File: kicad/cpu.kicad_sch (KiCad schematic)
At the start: 41 parts, among them U1 8088_Max_Mode, U12 8288, U13 SN74PAL16L81N, U145 PAL12L6, U16 7400, U2 8087, U3 XD184000xP, U4 8284, U5 74LS244, U77 74LS04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

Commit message: Fixes to clocks,  keyboard controller stuff.
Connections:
- net CLK_{8288} is gone; now on net CLK_{88}: U12.2 (CLK)
- net CLK_{88}: now also U77.9, U80.1 (I_{0}), U81.3 (I1a)
- net ~{RESET}: now also U80.14 (I/~{O_{3}})
- net ~{CLK_{88}}: now reaches U77.8
- net at U80.16 (I/~{O_{5}}): now also U79.6 (I_{5})
- net at U80.17 (I/~{O_{6}}): now also U79.7 (I_{6})
- net VR_1 renamed ~{RESET_{BRD}}
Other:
- moved on the sheet: U77D
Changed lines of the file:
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@@
 		(members "~{MEMW}" "~{MEMR}" "~{IOR}" "~{IOW}" "~{INTA}" "~{8237_{CS}}"
 			"~{8291_{CS}}" "~{8259_{CS}}" "~{8274_{CS}}" "~{8253_{CS}}" "~{KBDPAL_{CS}}"
-			"~{AEN}" "OSC" "PCLK"
+			"~{AEN}" "OSC" "CLK_{88}"
 		)
 	)
@@
 	)
 	(bus_entry
+		(at 104.14 368.3)
+		(size 2.54 2.54)
+		(stroke
+			(width 0)
+			(type default)
+		)
+	)
+	(bus_entry
 		(at 182.88 45.72)
 		(size 2.54 2.54)
@@
 	(wire
 		(pts
+			(xy 600.71 128.27) (xy 600.71 97.79)
+		)
+		(stroke
+			(width 0)
+			(type default)
+		)
+	)
+	(wire
+		(pts
 			(xy 15.24 120.65) (xy 15.24 228.6)
 		)
@@
 		)
 	)
+	(bus
+		(pts
+			(xy 104.14 252.73) (xy 104.14 368.3)
+		)
+		(stroke
+			(width 0)
+			(type default)
+		)
+	)
 	(wire
 		(pts
@@
 	(wire
 		(pts
+			(xy 684.53 96.52) (xy 684.53 128.27)
+		)
+		(stroke
+			(width 0)
+			(type default)
+		)
+	)
+	(wire
+		(pts
 			(xy 15.24 332.74) (xy 15.24 394.97)
 		)
@@
 	(wire
 		(pts
+			(xy 600.71 97.79) (xy 683.26 97.79)
+		)
+		(stroke
+			(width 0)
+			(type default)
+		)
+	)
+	(wire
+		(pts
 			(xy 290.83 139.7) (xy 298.45 139.7)
 		)
@@
 	(wire
 		(pts
+			(xy 599.44 130.81) (xy 599.44 96.52)
+		)
+		(stroke
+			(width 0)
+			(type default)
+		)
+	)
+	(wire
+		(pts
 			(xy 652.78 138.43) (xy 648.97 138.43)
 		)
@@
 		)
 	)
+	(wire
+		(pts
+			(xy 337.82 78.74) (xy 356.87 78.74)
+		)
+		(stroke
+			(width 0)
+			(type default)
+		)
+	)
 	(bus
 		(pts
@@
 	(wire
 		(pts
+			(xy 599.44 96.52) (xy 684.53 96.52)
+		)
+		(stroke
+			(width 0)
+			(type default)
+		)
+	)
+	(wire
+		(pts
 			(xy 248.92 295.91) (xy 237.49 295.91)
 		)
@@
 	(wire
 		(pts
+			(xy 645.16 115.57) (xy 652.78 115.57)
+		)
+		(stroke
+			(width 0)
+			(type default)
+		)
+	)
+	(wire
+		(pts
 			(xy 369.57 64.77) (xy 369.57 68.58)
 		)
@@
 	(wire
 		(pts
+			(xy 605.79 130.81) (xy 599.44 130.81)
+		)
+		(stroke
+			(width 0)
+			(type default)
+		)
+	)
+	(wire
+		(pts
 			(xy 212.09 264.16) (xy 205.74 264.16)
 		)
@@
 	(wire
 		(pts
+			(xy 673.1 120.65) (xy 695.96 120.65)
+		)
+		(stroke
+			(width 0)
+			(type default)
+		)
+	)
+	(wire
+		(pts
 			(xy 185.42 38.1) (xy 194.31 38.1)
 		)
@@
 	(wire
 		(pts
+			(xy 140.97 370.84) (xy 154.94 370.84)
+		)
+		(stroke
+			(width 0)
+			(type default)
+		)
+	)
+	(wire
+		(pts
 			(xy 116.84 265.43) (xy 128.27 265.43)
 		)
@@
 	(wire
 		(pts
+			(xy 683.26 97.79) (xy 683.26 125.73)
+		)
+		(stroke
+			(width 0)
+			(type default)
+		)
+	)
+	(wire
+		(pts
 			(xy 290.83 48.26) (xy 298.45 48.26)
 		)
@@
 	(wire
 		(pts
+			(xy 106.68 370.84) (xy 125.73 370.84)
+		)
+		(stroke
+			(width 0)
+			(type default)
+		)
+	)
+	(wire
+		(pts
 			(xy 16.51 568.96) (xy 44.45 568.96)
 		)
@@
 	(wire
 		(pts
+			(xy 605.79 128.27) (xy 600.71 128.27)
+		)
+		(stroke
+			(width 0)
+			(type default)
+		)
+	)
+	(wire
+		(pts
 			(xy 198.12 339.09) (xy 198.12 342.9)
 		)
@@
 	(wire
 		(pts
+			(xy 684.53 128.27) (xy 673.1 128.27)
+		)
+		(stroke
+			(width 0)
+			(type default)
+		)
+	)
+	(wire
+		(pts
+			(xy 683.26 125.73) (xy 673.1 125.73)
+		)
+		(stroke
+			(width 0)
+			(type default)
+		)
+	)
+	(wire
+		(pts
 			(xy 248.92 293.37) (xy 237.49 293.37)
 		)
@@
 		)
 	)
+	(label "CLK_{88}"
+		(at 337.82 78.74 0)
+		(effects
+			(font
+				(size 1.27 1.27)
+			)
+			(justify left bottom)
+		)
+	)
 	(label "AD6"
 		(at 176.53 265.43 0)
@@
 		)
 	)
+	(label "~{CLK_{88}}"
+		(at 152.4 370.84 180)
+		(effects
+			(font
+				(size 1.27 1.27)
+			)
+			(justify right bottom)
+		)
+	)
+	(label "CLK_{88}"
+		(at 187.96 377.19 0)
+		(effects
+			(font
+				(size 1.27 1.27)
+			)
+			(justify left bottom)
+		)
+	)
 	(label "RESET"
 		(at 118.11 255.27 0)
@@
 		)
 	)
+	(label "CLK_{88}"
+		(at 645.16 115.57 0)
+		(effects
+			(font
+				(size 1.27 1.27)
+			)
+			(justify left bottom)
+		)
+	)
 	(label "A10"
 		(at 172.72 63.5 0)
@@
 		)
 	)
+	(label "CLK_{88}"
+		(at 118.11 370.84 0)
+		(effects
+			(font
+				(size 1.27 1.27)
+			)
+			(justify left bottom)
+		)
+	)
 	(label "A16"
 		(at 262.89 55.88 180)
@@
 		)
 	)
-	(label "CLK_{8288}"
-		(at 187.96 377.19 0)
-		(effects
-			(font
-				(size 1.27 1.27)
-			)
-			(justify left bottom)
-		)
-	)
 	(label "~{Z_HALT}"
 		(at 124.46 88.9 0)
@@
 		)
 	)
+	(label "~{RESET}"
+		(at 695.96 120.65 180)
+		(effects
+			(font
+				(size 1.27 1.27)
+			)
+			(justify right bottom)
+		)
+	)
 	(label "AD7"
 		(at 209.55 311.15 180)
@@
 		)
 	)
-	(global_label "VR_1"
+	(global_label "~{RESET_{BRD}}"
 		(shape input)
 		(at 532.13 90.17 180)
@@
 	(symbol
 		(lib_id "74xx:74LS04")
-		(at 325.12 364.49 0)
+		(at 133.35 370.84 0)
 		(unit 4)
 		(exclude_from_sim no)
@@
 		(fields_autoplaced yes)
 		(property "Reference" "U77"
-			(at 325.12 355.6 0)
+			(at 133.35 361.95 0)
 			(effects
 				(font
@@
 		)
 		(property "Value" "74LS04"
-			(at 325.12 358.14 0)
+			(at 133.35 364.49 0)
 			(effects
 				(font
@@
 		)
 		(property "Footprint" "Package_DIP:DIP-14_W7.62mm"
-			(at 325.12 364.49 0)
+			(at 133.35 370.84 0)
 			(effects
 				(font
@@
 		)
 		(property "Datasheet" "http://www.ti.com/lit/gpn/sn74LS04"
-			(at 325.12 364.49 0)
+			(at 133.35 370.84 0)
 			(effects
 				(font
@@
 		)
 		(property "Description" "Hex Inverter"
-			(at 325.12 364.49 0)
+			(at 133.35 370.84 0)
 			(effects
 				(font
@@
 		)
 		(property "seq_partno" ""
-			(at 325.12 364.49 0)
+			(at 133.35 370.84 0)
 			(effects
 				(font
@@
 		)
 		(property "seq_coord" ""
-			(at 325.12 364.49 0)
+			(at 133.35 370.84 0)
 			(effects
 				(font
@@
 		)
 		(property "seq_silkscreen" ""
-			(at 325.12 364.49 0)
+			(at 133.35 370.84 0)
 			(effects
 				(font
@@
 		)
 		(property "seq_sharpie" ""
-			(at 325.12 364.49 0)
+			(at 133.35 370.84 0)
 			(effects
 				(font
@@
 		)
 		(property "seq_notes" ""
-			(at 325.12 364.49 0)
+			(at 133.35 370.84 0)
 			(effects
 				(font

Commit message: update kicad project
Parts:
- removed unit 5 of U77
- added R17B1: ??Ω, seequa_footprints:R_Seequa_Resistor, symbol Device:R_Small
- added U89: 74LS04, Package_DIP:DIP-14_W7.62mm, symbol 74xx:74LS04
- C1, C2, C89, X1: seq_coord (none) -> E5
- C115: seq_coord (none) -> D3
- C116: seq_coord (none) -> C9
- C117: seq_coord (none) -> D7
- C118: seq_coord (none) -> E12
- C3, RN2: seq_coord (none) -> F2
- C4, SP2: seq_coord (none) -> G0
- C99: seq_coord (none) -> I2
- D1, R4: seq_coord (none) -> E9
- R1, R2: seq_coord (none) -> D5
- R17: seq_coord (none) -> G4
- R3: seq_coord (none) -> F4
- RN1: seq_coord (none) -> E4
- U1: seq_coord (none) -> E1
- U12: seq_coord (none) -> H4; seq_notes (none) -> Intel 8288 Bus Controller
- U13: value SN74PAL16L81N -> PAL16L8; seq_coord (none) -> F3; seq_notes (none) -> CPU Status Translator
- U145: seq_coord (none) -> G11; seq_notes (none) -> NMI & LPT Interrupt Control
- U16: seq_coord (none) -> C3; seq_silkscreen (none) -> 00
- U2: seq_coord (none) -> E3
- U3: seq_coord (none) -> G1; seq_silkscreen (none) -> Z80A
- U4: seq_coord (none) -> D4
- U5: seq_coord (none) -> G3
- U77: seq_coord (none) -> F5; seq_silkscreen (none) -> LS04
- U78: seq_coord (none) -> I1; seq_notes (none) -> Address Latch 1
- U79: value SN74PAL16L81N -> PAL16R8; symbol Logic_Programmable:PAL16L8 -> seequa:PAL16R6; seq_coord (none) -> G5; seq_notes (none) -> DMA Logic PAL 2; seq_partno SN74PAL16L81N -> (none)
- U80: value AMPAL16R8 -> PAL16R8; symbol Logic_Programmable:PAL16L8 -> seequa:PAL16R6; seq_coord (none) -> G6; seq_notes (none) -> CPU eXchange Control; seq_partno (none) -> AMPAL16R8; seq_silkscreen CPX5 -> CPX
- U81: seq_coord (none) -> G7; seq_notes (none) -> Address Enable Mux; seq_silkscreen (none) -> LS157
- U83: seq_coord (none) -> I4; seq_notes (none) -> Address Latch 2
- U90: seq_coord (none) -> E6; seq_notes (none) -> Data Bus Driver; seq_silkscreen (none) -> LS245
- U91: seq_coord (none) -> E7; seq_notes (none) -> Address Latch 0; seq_silkscreen (none) -> LS373
- U92: value 74S273 -> 74LS273; seq_coord (none) -> E8; seq_notes (none) -> Option Register 1; seq_port (none) -> 3DDh; seq_silkscreen (none) -> LS273
- U93: seq_coord (none) -> E11
- U94: seq_coord (none) -> E12; seq_silkscreen (none) -> LS173
- U95: seq_coord (none) -> G9; seq_silkscreen (none) -> LS107
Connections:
- net DCON_S is gone; now on net ~{88_PRIMARY}: U80.18 (~{O_{7}}), U81.1 (S)
- net NMI_P16 is gone; now on net ~{LPT_S_ACK}: U145.16 (~{O_{4}})
- net OPT1_B1 is gone; now on net CPX_P7: U92.12 (Q4)
- net QD0 is gone; now on net CPX_P6: U80.6 (I_{5})
- net S0 is gone; now on net ~{S0}: U13.17 (I/~{O_{6}})
- net S1 is gone; now on net ~{S1}: U13.16 (I/~{O_{5}})
- net S2 is gone; now on net ~{S2}: U13.15 (I/~{O_{4}})
- net ~{Z80_AEN} is gone; now on net ~{Z_AEN}: U81.9 (Zc)
- net ~{Z_WAIT} is gone; now on net ~{DMA_WAIT}: U3.24 (~{WAIT})
- net +5V: now also U81.10 (I1c), U81.16 (VCC), U81.5 (I0b), U95.13 (~{R}), R17B1.1
- net GND: now also U81.15 (E)
- net INTR: now also U80.3 (I_{2})
- net PCLK: now also U81.2 (I0a)
- net ~{CLK_{88}}: now also U79.1 (I_{0})
- net ~{RESET_{BRD}}: now also U92.1 (~{Mr})
- net ~{SP}/~{EN}: now also RN1.6 (R5.2)
- net ~{Z_BUSACK}: now also U79.4 (I_{3})
- net ~{LOCK}: now reaches U80.2 (I_{1})
- net ~{LOCK}: now also U1.29 (~{LOCK}), U79.3 (I_{2}), R17B1.2
- net CPX_P7: now reaches U80.7 (I_{6})
- net ~{HOLDA}: now reaches U79.14 (~{O_{3}})
- net ~{HOLDA}: now also U89.11
- net HRQ: now reaches U79.2 (I_{1})
- net ~{88_PRIMARY}: now reaches U79.8 (I_{7})
- net ~{BHE}: now reaches RN1.4 (R3.2), U2.34 (~{BHE}/S7)
- net ~{PARITY_CLK}: now reaches U95.9 (C)
- net DMA_AEN: now reaches U93.11 (~{Er})
- net ~{LPT_ACK}: now reaches U145.1 (I_{0})
- net ~{LPT_S_ACK}: now reaches U145.19 (I_{11})
- net NMI_P3: now reaches U145.3 (I_{2})
- net NMI_P2 renamed LPT_SELECT_IN
- net NMI_PAL_{I9} renamed ~{IO_CH_CK}
- net OPT1_B0 renamed CPX_P6
- net OPT1_B7 renamed WIRE_CUT
- net QD7 renamed ~{CPU_SWAP_STR}
- net ~{IOCK_{EN}} renamed ~{IO_CK_{EN}}
- new net HOLDA: U89.10
- no-connect marks 13 -> 22
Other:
- note added: "From Video Register Decoder"
- note added: "To DCON PAL (Page #9)"
- note added: "To KBD PAL"
- moved on the sheet: C115, C116, C117, C118, C2, C3, C4, C89, C99, R1, R17, R2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

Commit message: More updates
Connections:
- net PCLK: now also U95.12 (C)
- net ~{BRD_CK_{EN}}: now reaches U95.10 (~{R})
- net NMI: now reaches U1.17 (NMI), U77.12
- net OPT1_B3 renamed NMI_ON_INT
- net OPT1_B4 renamed 88_NMI_{EN}
- net OPT1_B5 renamed Z80_NMI_{EN}
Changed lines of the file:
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@@
 	(wire
 		(pts
+			(xy 490.22 347.98) (xy 490.22 345.44)
+		)
+		(stroke
+			(width 0)
+			(type default)
+		)
+	)
+	(wire
+		(pts
 			(xy 49.53 156.21) (xy 49.53 158.75)
 		)
@@
 	(wire
 		(pts
+			(xy 469.9 347.98) (xy 490.22 347.98)
+		)
+		(stroke
+			(width 0)
+			(type default)
+		)
+	)
+	(wire
+		(pts
 			(xy 309.88 170.18) (xy 320.04 170.18)
 		)
@@
 	(wire
 		(pts
+			(xy 25.4 148.59) (xy 41.91 148.59)
+		)
+		(stroke
+			(width 0)
+			(type default)
+		)
+	)
+	(wire
+		(pts
 			(xy 74.93 69.85) (xy 83.82 69.85)
 		)
@@
 		)
 	)
-	(label "OPT1_B4"
+	(label "88_NMI_{EN}"
 		(at 377.19 339.09 0)
 		(effects
@@
 		)
 	)
-	(label "OPT1_B4"
+	(label "88_NMI_{EN}"
 		(at 251.46 295.91 180)
 		(effects
@@
 		)
 	)
+	(label "NMI"
+		(at 116.84 156.21 0)
+		(effects
+			(font
+				(size 1.27 1.27)
+			)
+			(justify left bottom)
+		)
+	)
 	(label "~{MEMW}"
 		(at 251.46 356.87 180)
@@
 		)
 	)
+	(label "PCLK"
+		(at 25.4 148.59 0)
+		(effects
+			(font
+				(size 1.27 1.27)
+			)
+			(justify left bottom)
+		)
+	)
 	(label "XA18"
 		(at 340.36 186.69 180)
@@
 		)
 	)
-	(label "OPT1_B3"
+	(label "NMI_ON_INT"
 		(at 377.19 341.63 0)
 		(effects
@@
 		)
 	)
-	(label "OPT1_B5"
+	(label "Z80_NMI_{EN}"
 		(at 251.46 308.61 180)
 		(effects
@@
 		)
 	)
-	(label "OPT1_B3"
+	(label "NMI_ON_INT"
 		(at 251.46 306.07 180)
 		(effects
@@
 		)
 	)
+	(global_label "~{BRD_CK_{EN}}"
+		(shape input)
+		(at 469.9 347.98 180)
+		(fields_autoplaced yes)
+		(effects
+			(font
+				(size 1.27 1.27)
+			)
+			(justify right)
+		)
+		(property "Intersheetrefs" "${INTERSHEET_REFS}"
+			(at 457.5628 347.98 0)
+			(effects
+				(font
+					(size 1.27 1.27)
+				)
+				(justify right)
+				(hide yes)
+			)
+		)
+	)
 	(global_label "~{IO_CH_CK}"
 		(shape input)
@@
 		)
 	)
-	(global_label "OPT1_B5"
+	(global_label "Z80_NMI_{EN}"
 		(shape input)
 		(at 377.19 336.55 180)
@@
 			)
 		)
+		(property "seq_port" ""
+			(at 518.16 238.76 0)
+			(effects
+				(font
+					(size 1.27 1.27)
+				)
+				(hide yes)
+			)
+		)
 		(pin "4"
 		)
@@
 			(effects
 				(font
-					(size 1.27 1.27)
+					(size 1.5 1.5)
+					(thickness 0.254)
+					(bold yes)
 				)
 				(justify left)

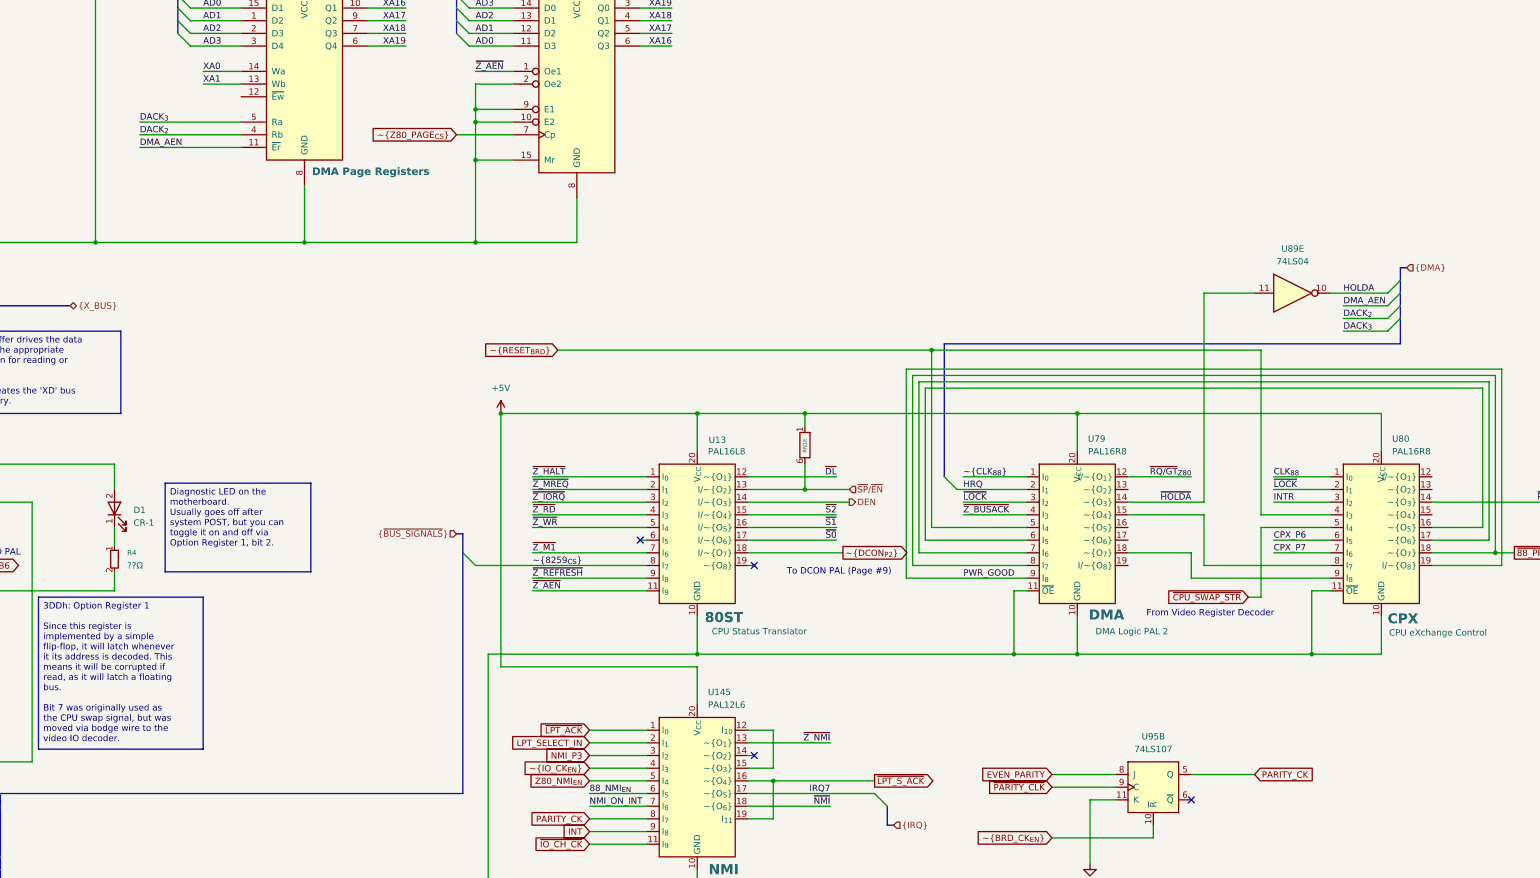
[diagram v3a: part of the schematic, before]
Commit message: Add parallel port, game port
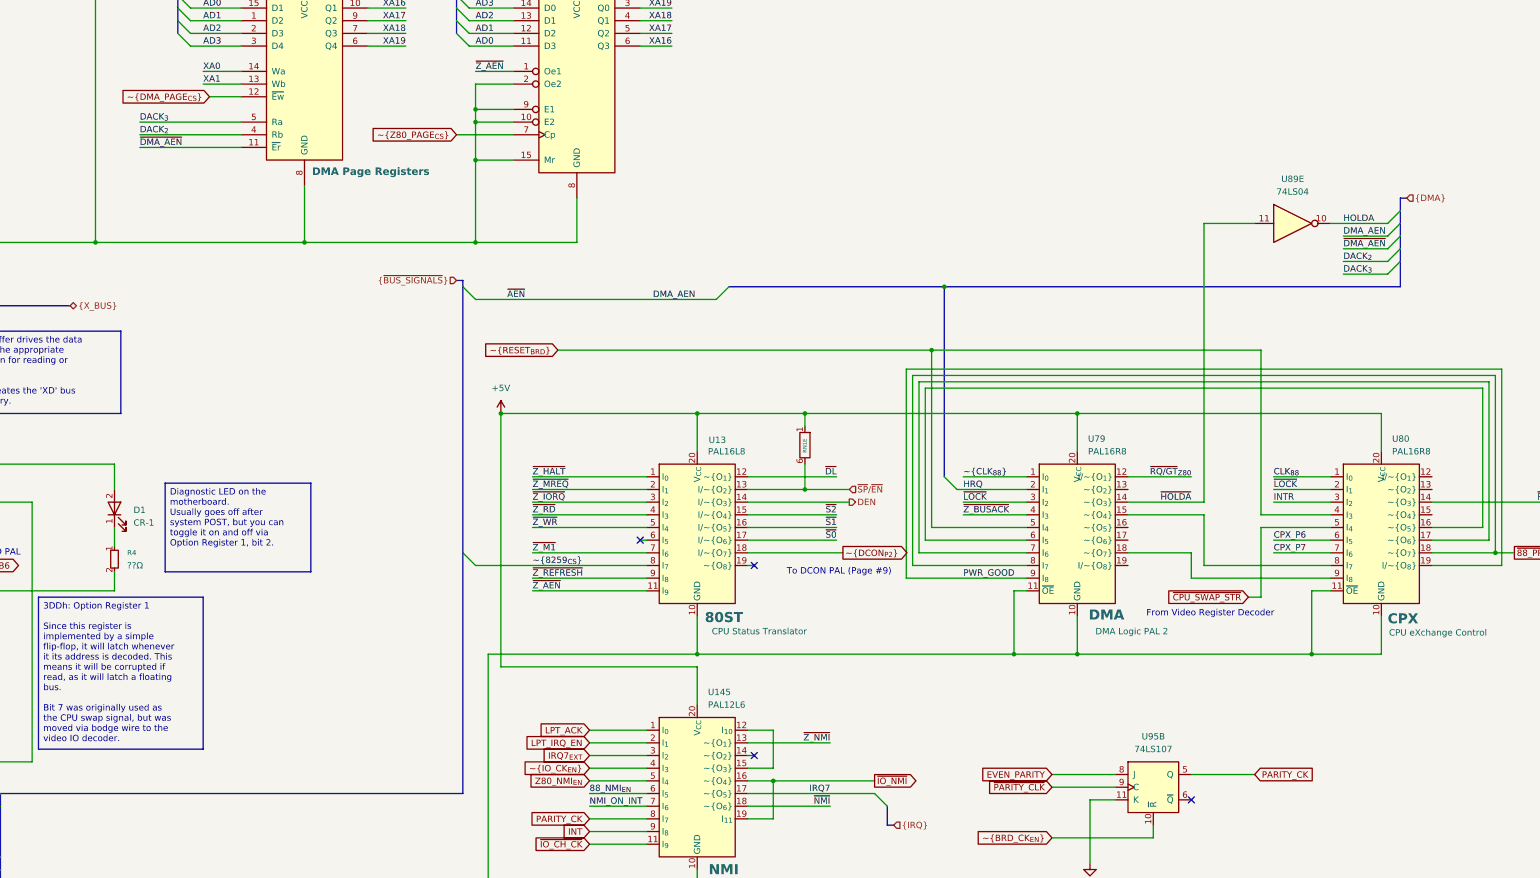
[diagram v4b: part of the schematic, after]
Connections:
- net ~{AEN} is gone; now on net DMA_AEN: U12.6 (~{AEN}), U78.1 (OE), U81.11 (I0c), U81.6 (I1b)
- net DMA_AEN: no longer U93.11 (~{Er})
- net ~{DMA_PAGE_{CS}}: now reaches U93.12 (~{Ew})
- net LPT_SELECT_IN renamed LPT_IRQ_EN
- net NMI_P3 renamed IRQ7_{EXT}
- net ~{LPT_ACK} renamed LPT_ACK
- net ~{LPT_S_ACK} renamed ~{IO_NMI}
- new net ~{DMA_AEN}: U93.11 (~{Er})
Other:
- moved on the sheet: U89E

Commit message: Updates, chameleon logo
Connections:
- net ~{Z_BUSREQ}: now also U80.15 (~{O_{4}})
- net INT renamed INT_{87}
- net NMI_ON_INT renamed 87_NMI_{EN}
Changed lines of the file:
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@@
 		(members "~{MEMW}" "~{MEMR}" "~{IOR}" "~{IOW}" "~{INTA}" "~{8237_{CS}}"
 			"~{8291_{CS}}" "~{8259_{CS}}" "~{8274_{CS}}" "~{8253_{CS}}" "~{KBDPAL_{CS}}"
-			"~{AEN}" "OSC" "CLK_{88}" "ALE" "~{INTA}" "~{LPT_{CS}}" "~{VIDEO_DECODER_{CS}}"
+			"~{AEN}" "OSC" "CLK_{88}" "ALE" "~{INTA}" "~{LPT_{CS}}" "~{VIDEO_DECODER_{EN}}"
 			"~{CRTC_{CS}}" "~{DMA_PAGE_{CS}}" "~{FDC_{CS}}"
 		)
@@
 	(wire
 		(pts
-			(xy 464.82 293.37) (xy 441.96 293.37)
-		)
-		(stroke
-			(width 0)
-			(type default)
-		)
-	)
-	(wire
-		(pts
 			(xy 278.13 76.2) (xy 234.95 76.2)
 		)
@@
 	(wire
 		(pts
+			(xy 441.96 293.37) (xy 464.82 293.37)
+		)
+		(stroke
+			(width 0)
+			(type default)
+		)
+	)
+	(wire
+		(pts
 			(xy 450.85 278.13) (xy 464.82 278.13)
 		)
@@
 	(wire
 		(pts
+			(xy 546.1 283.21) (xy 572.77 283.21)
+		)
+		(stroke
+			(width 0)
+			(type default)
+		)
+	)
+	(wire
+		(pts
 			(xy 185.42 254) (xy 212.09 254)
 		)
@@
 		)
 	)
+	(label "Z80_NMI_{EN}"
+		(at 377.19 336.55 0)
+		(effects
+			(font
+				(size 1.27 1.27)
+			)
+			(justify left bottom)
+		)
+	)
 	(label "IRQ7"
 		(at 425.45 339.09 180)
@@
 		)
 	)
+	(label "~{88_PRIMARY}"
+		(at 452.12 293.37 0)
+		(effects
+			(font
+				(size 1.27 1.27)
+			)
+			(justify left bottom)
+		)
+	)
 	(label "~{INTA}"
 		(at 251.46 369.57 180)
@@
 		)
 	)
+	(label "~{Z_BUSREQ}"
+		(at 572.77 283.21 180)
+		(effects
+			(font
+				(size 1.27 1.27)
+			)
+			(justify right bottom)
+		)
+	)
 	(label "XA1"
 		(at 222.25 48.26 0)
@@
 		)
 	)
-	(label "INT"
+	(label "INT_{87}"
 		(at 175.26 321.31 180)
 		(effects
@@
 		)
 	)
-	(label "NMI_ON_INT"
+	(label "87_NMI_{EN}"
 		(at 377.19 341.63 0)
 		(effects
@@
 		)
 	)
-	(label "NMI_ON_INT"
+	(label "87_NMI_{EN}"
 		(at 251.46 306.07 180)
 		(effects
@@
 		)
 	)
-	(global_label "Z80_NMI_{EN}"
-		(shape input)
-		(at 377.19 336.55 180)
-		(fields_autoplaced yes)
-		(effects
-			(font
-				(size 1.27 1.27)
-			)
-			(justify right)
-		)
-		(property "Intersheetrefs" "${INTERSHEET_REFS}"
-			(at 370.3948 336.55 0)
-			(effects
-				(font
-					(size 1.27 1.27)
-				)
-				(justify right)
-				(hide yes)
-			)
-		)
-	)
 	(global_label "PARITY_CK"
 		(shape input)
@@
 		)
 	)
-	(global_label "INT"
+	(global_label "INT_{87}"
 		(shape input)
 		(at 377.19 346.71 180)
